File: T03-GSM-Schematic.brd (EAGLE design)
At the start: 33.9 x 80.5 mm, 20 parts, among them IC1 788TV, J1 POWER_JACKPTH_BREAD, J2 AVR, Q2 16M, U1 ATMEGA328P-PU

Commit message: Added terminal points for GSM module
5V and GND
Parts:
- removed RX, TX: (no value), wirepad:2,54/0,9
- added SV1: GSM-header, con-lstb:MA04-1
- moved C6 0.93 mm to (19.8, 57.9)
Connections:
- removed net N$1: TX.1, U1.4
- removed net N$12: RX.1, U1.5
- new net RX: SV1.4, U1.5
- new net TX: SV1.3, U1.4
- net 5V: now also SV1.2
- net GND: now also SV1.1
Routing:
- net N$1: track 10.9 -> 0.00 mm
- net N$12: track 9.41 -> 0.00 mm
- net TX: track 0.00 -> 7.75 mm
- net RX: track 0.00 -> 7.35 mm
- net N$10: track 38.9 -> 44.1 mm
- net 5V: track 70.1 -> 74.7 mm
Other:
- board text added: "5V"
- board text added: "GND"
- board text added: "RX"
- board text added: "TX"

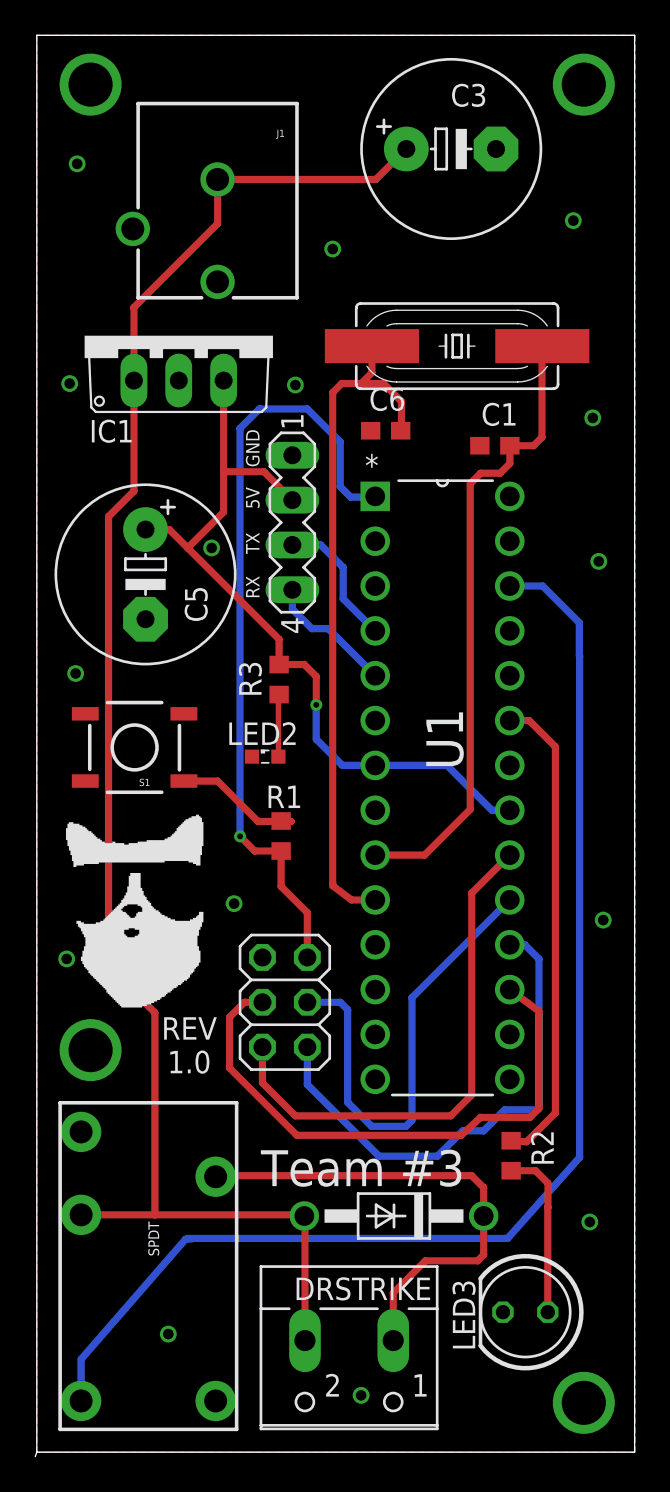
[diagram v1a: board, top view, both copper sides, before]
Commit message: Moved the power jack position
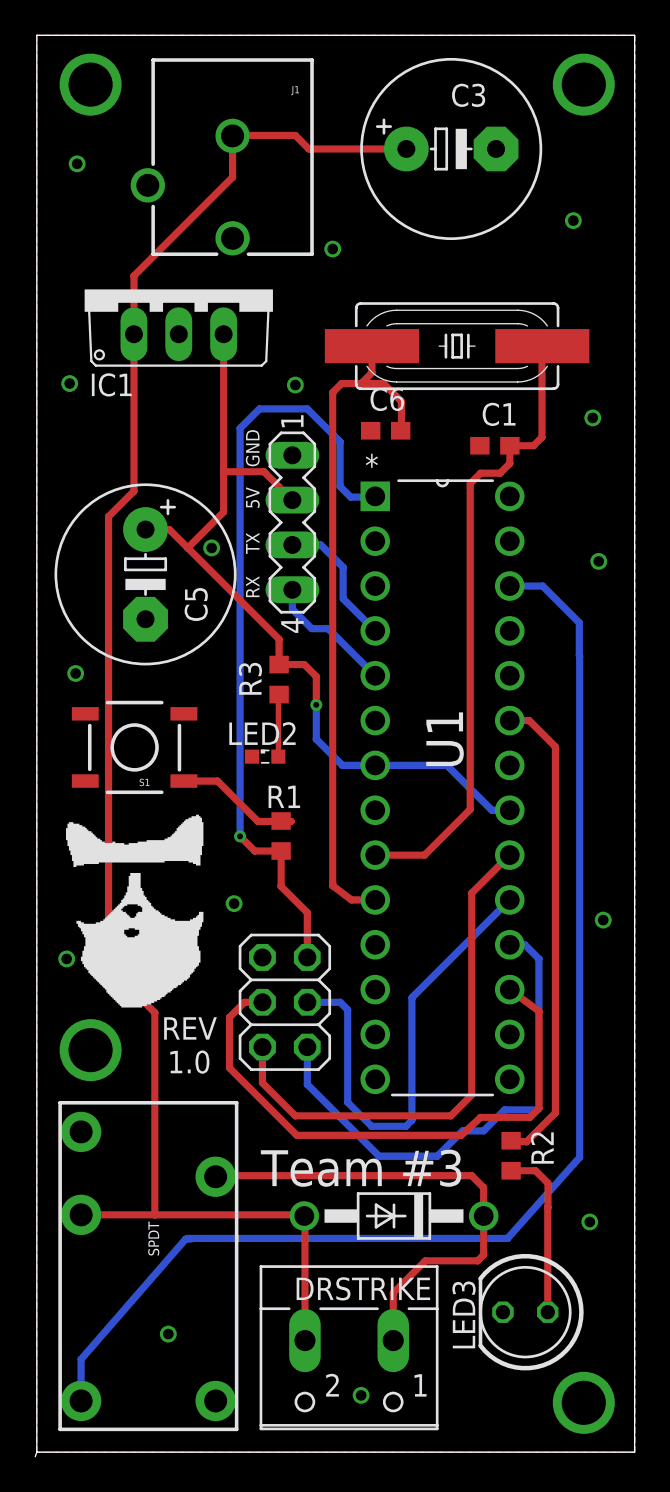
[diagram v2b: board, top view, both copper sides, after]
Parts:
- moved IC1 2.62 mm to (8.04, 65.9)
- moved J1 2.61 mm to (11.1, 82.5)
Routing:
- net 5V: track 74.7 -> 77.3 mm
- net 12V: track 93.5 -> 95.0 mm
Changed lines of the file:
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@@
 </class>
 </classes>
-<designrules name="oshpark-2layer *">
+<designrules name="oshpark-2layer">
 <description language="de">&lt;b&gt;EAGLE Design Rules&lt;/b&gt;
 &lt;p&gt;
@@
 <param name="mdPadVia" value="6mil"/>
 <param name="mdViaVia" value="6mil"/>
-<param name="mdSmdPad" value="0mil"/>
-<param name="mdSmdVia" value="0mil"/>
-<param name="mdSmdSmd" value="0mil"/>
+<param name="mdSmdPad" value="6mil"/>
+<param name="mdSmdVia" value="6mil"/>
+<param name="mdSmdSmd" value="6mil"/>
 <param name="mdViaViaSameLayer" value="8mil"/>
 <param name="mnLayersViaInSmd" value="2"/>
@@
 <attribute name="NAME" x="22.38278125" y="9.884484375" size="1.27" layer="25" ratio="10" rot="R180"/>
 </element>
-<element name="J1" library="SparkFun-Connectors" package="POWER_JACK_PTH_BREAD" value="POWER_JACKPTH_BREAD" x="10.237971875" y="79.9891875" rot="R180">
-<attribute name="PROD_ID" value="PRT-10811" x="10.237971875" y="79.9891875" size="1.778" layer="27" rot="R180" display="off"/>
+<element name="J1" library="SparkFun-Connectors" package="POWER_JACK_PTH_BREAD" value="POWER_JACKPTH_BREAD" x="11.090225" y="82.45708125" rot="R180">
+<attribute name="PROD_ID" value="PRT-10811" x="11.090225" y="82.45708125" size="1.778" layer="27" rot="R180" display="off"/>
 </element>
 <element name="LED2" library="led" package="SML0603" value="" x="12.935275" y="39.39726875" smashed="yes">
@@
 </element>
 <element name="J2" library="pinhead" package="2X03" value="AVR" x="14.05326875" y="25.482121875" smashed="yes" rot="R90"/>
-<element name="IC1" library="linear" package="TO220V" value="788TV" x="8.042528125" y="63.239675"/>
+<element name="IC1" library="linear" package="TO220V" value="788TV" x="8.042528125" y="65.864078125"/>
 <element name="SV1" library="con-lstb" package="MA04-1" value="GSM-header" x="14.47655" y="52.657396875" smashed="yes" rot="R270">
 <attribute name="MF" value="" x="14.47655" y="52.657396875" size="1.778" layer="27" rot="R270" display="off"/>
@@
 </polygon>
 <polygon width="0.4064" layer="16">
-<vertex x="-0.000003125" y="80.253975"/>
-<vertex x="0" y="-0.000003125"/>
+<vertex x="0" y="80.253975"/>
+<vertex x="0" y="0"/>
 <vertex x="33.88194375" y="0"/>
 <vertex x="33.881946875" y="80.253971875"/>
@@
 <contactref element="IC1" pad="3"/>
 <wire x1="10.582528125" y1="53.250259375" x2="8.550478125" y2="51.218209375" width="0.4064" layer="1"/>
-<wire x1="10.582528125" y1="60.699675" x2="10.582528125" y2="55.535778125" width="0.4064" layer="1"/>
+<wire x1="10.582528125" y1="63.324078125" x2="10.582528125" y2="55.535778125" width="0.4064" layer="1"/>
 <wire x1="10.582528125" y1="55.535778125" x2="10.582528125" y2="53.250259375" width="0.4064" layer="1"/>
 <wire x1="15.83108125" y1="42.3291" x2="15.83108125" y2="43.937609375" width="0.4064" layer="1"/>
@@
 <wire x1="15.19" y1="6.32" x2="15.19" y2="13.33930625" width="0.4064" layer="1"/>
 <wire x1="15.19" y1="13.33930625" x2="15.153309375" y2="13.375996875" width="0.4064" layer="1"/>
-<wire x1="5.502528125" y1="60.699675" x2="5.502528125" y2="64.847925" width="0.4064" layer="1"/>
-<wire x1="5.502528125" y1="64.847925" x2="10.24364375" y2="69.589040625" width="0.4064" layer="1"/>
-<wire x1="10.24364375" y1="69.589040625" x2="10.24364375" y2="72.083515625" width="0.4064" layer="1"/>
-<wire x1="10.24364375" y1="72.083515625" x2="10.237971875" y2="72.0891875" width="0.4064" layer="1"/>
-<wire x1="10.237971875" y1="72.0891875" x2="19.20609375" y2="72.0891875" width="0.4064" layer="1"/>
-<wire x1="19.20609375" y1="72.0891875" x2="20.933709375" y2="73.816803125" width="0.4064" layer="1"/>
 <wire x1="2.51" y1="13.441" x2="6.687996875" y2="13.441" width="0.4064" layer="1"/>
 <wire x1="6.687996875" y1="13.441" x2="15.08830625" y2="13.441" width="0.4064" layer="1"/>
 <wire x1="15.08830625" y1="13.441" x2="15.153309375" y2="13.375996875" width="0.4064" layer="1"/>
-<wire x1="5.502528125" y1="60.699675" x2="5.502528125" y2="54.43496875" width="0.4064" layer="1"/>
+<wire x1="5.502528125" y1="63.324078125" x2="5.502528125" y2="54.43496875" width="0.4064" layer="1"/>
 <wire x1="5.502528125" y1="54.43496875" x2="4.06359375" y2="52.996034375" width="0.4064" layer="1"/>
 <wire x1="4.06359375" y1="52.996034375" x2="4.06359375" y2="27.5139125" width="0.4064" layer="1"/>
 <wire x1="4.06359375" y1="27.5139125" x2="6.687996875" y2="24.889509375" width="0.4064" layer="1"/>
 <wire x1="6.687996875" y1="24.889509375" x2="6.687996875" y2="13.441" width="0.4064" layer="1"/>
+<wire x1="20.933709375" y1="73.816803125" x2="15.412940625" y2="73.816803125" width="0.4064" layer="1"/>
+<wire x1="15.412940625" y1="73.816803125" x2="14.64586875" y2="74.583875" width="0.4064" layer="1"/>
+<wire x1="14.64586875" y1="74.583875" x2="11.11701875" y2="74.583875" width="0.4064" layer="1"/>
+<wire x1="5.502528125" y1="63.324078125" x2="5.502528125" y2="66.625746875" width="0.4064" layer="1"/>
+<wire x1="5.502528125" y1="66.625746875" x2="11.090225" y2="72.21344375" width="0.4064" layer="1"/>
+<wire x1="11.090225" y1="72.21344375" x2="11.090225" y2="74.55708125" width="0.4064" layer="1"/>
+<wire x1="11.090225" y1="74.55708125" x2="11.11701875" y2="74.583875" width="0" layer="19" extent="1-1"/>
 </signal>
 <signal name="N$16">
